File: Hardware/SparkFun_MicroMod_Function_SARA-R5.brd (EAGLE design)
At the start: 37.5 x 65 mm, 119 parts, among them IC2 SN74AVC4T774PW, J1 MICROMOD_FUNCTION_STANDARD, J2 U.FL, J4 U.FL, J9 NANO_SIM, Q2 310mA/60V/1.6Ω, Q3 310mA/60V/1.6Ω, Q5 310mA/60V/1.6Ω, Q6 310mA/60V/1.6Ω, U1 SARA-R510M8S, U11 74HC1G04, U3 3.3V, U4 EEPROM, U8 AP7361C-33FGE

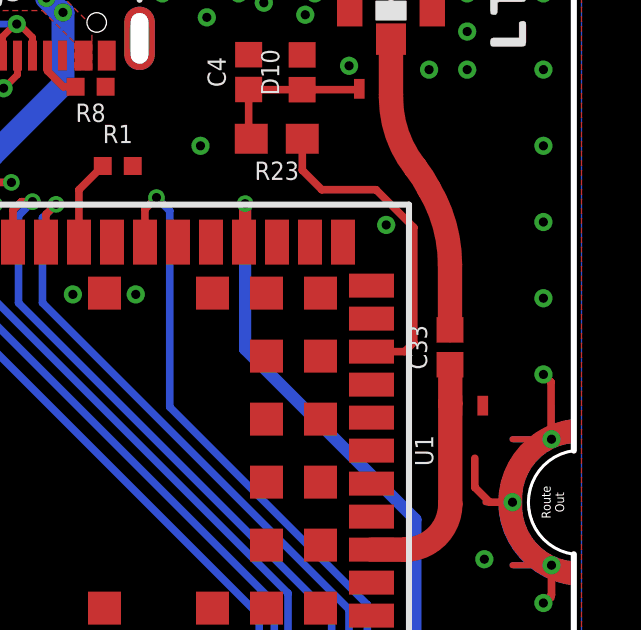
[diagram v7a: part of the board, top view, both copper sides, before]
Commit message: library work
-switching some parts over to SFE libraries
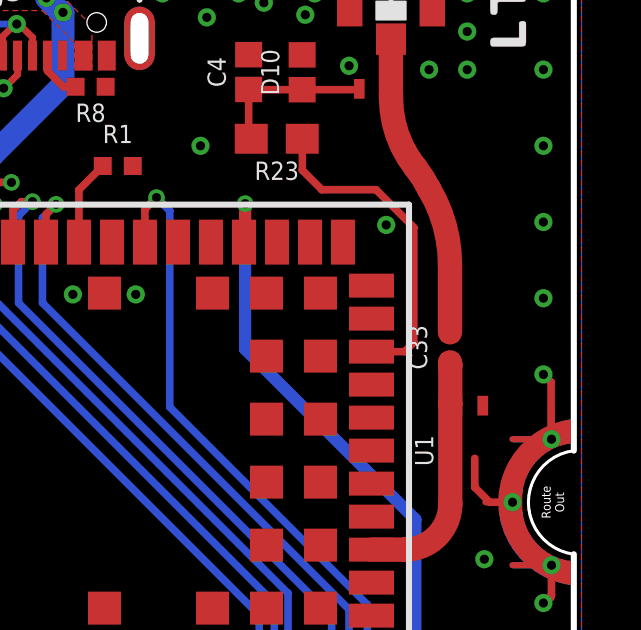
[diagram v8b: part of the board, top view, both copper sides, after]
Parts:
- C33: device New_Parts:0402 -> SparkFun-Capacitors:0402-TIGHT
- C4: device New_Parts:0402 -> SparkFun-Capacitors:0402
- D10, D4: value PESD0402 -> PESD0402-0402; device New_Parts:0402 -> SparkFun-DiscreteSemi:0402
- D15: device ublox:SOT23-6L -> SparkFun-DiscreteSemi:SOT23-6L
- IC2: device New_Parts:SOP65P640X120-16N -> SparkFun-IC-Comms:SOP65P640X120-16N
- L2: device New_Parts:0402_COILCRAFT -> SparkFun-Coils:0402_COILCRAFT
